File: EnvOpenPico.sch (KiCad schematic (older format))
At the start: 36 parts, among them J2 Conn_01x02, J3 Conn_02x18_Odd_Even, J4 Conn_02x18_Odd_Even, J5 Conn_01x03_Male, U1 NCP1117-3.3_SOT223, U2 W25Q16JVSSIQ, U3 RP2040, X1 XO32

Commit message: Changed Regulator for one with an enable pin
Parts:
- added R7: R100K, Resistor_SMD:R_0201_0603Metric, symbol Device:R
- R5, R6: footprint (none) -> Resistor_SMD:R_0201_0603Metric
- U1: value NCP1117-3.3_SOT223 -> SPX3819M5-L-3-3; footprint Package_TO_SOT_SMD:SOT-23 -> Package_TO_SOT_SMD:SOT-23-5; symbol Regulator_Linear:NCP1117-3.3_SOT223 -> Regulator_Linear:SPX3819M5-L-3-3
- U2: footprint Package_SO:SOIC-8_5.23x5.23mm_P1.27mm -> W25Q16JVSSIQ:SOIC127P790X216-8N
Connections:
- net labels added: 3V3_EN
- wire segments 182 -> 185
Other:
- moved on the sheet: C1
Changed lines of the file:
@@
 $EndComp
 $Comp
-L Regulator_Linear:NCP1117-3.3_SOT223 U1
+L Regulator_Linear:SPX3819M5-L-3-3 U1
 U 1 1 5F04C8B7
-P 3000 1750
-F 0 "U1" H 3000 1992 50  0000 C CNN
-F 1 "NCP1117-3.3_SOT223" H 3000 1901 50  0000 C CNN
-F 2 "Package_TO_SOT_SMD:SOT-23" H 3000 1950 50  0001 C CNN
-F 3 "http://www.onsemi.com/pub_link/Collateral/NCP1117-D.PDF" H 3100 1500 50  0001 C CNN
-	1    3000 1750
+P 3000 1850
+F 0 "U1" H 3000 2092 50  0000 C CNN
+F 1 "SPX3819M5-L-3-3" H 3000 2200 50  0000 C CNN
+F 2 "Package_TO_SOT_SMD:SOT-23-5" H 3000 2050 50  0001 C CNN
+F 3 "~" H 3100 1600 50  0001 C CNN
+	1    3000 1850
 	1    0    0    -1
 $EndComp
@@
 L power:GND #PWR05
 U 1 1 5F06A60B
-P 3000 2100
-F 0 "#PWR05" H 3000 1850 50  0001 C CNN
-F 1 "GND" H 2850 2050 50  0000 C CNN
-F 2 "" H 3000 2100 50  0001 C CNN
-F 3 "" H 3000 2100 50  0001 C CNN
-	1    3000 2100
-	1    0    0    -1
-$EndComp
-Wire Wire Line
-	3000 2050 3000 2100
+P 3000 2150
+F 0 "#PWR05" H 3000 1900 50  0001 C CNN
+F 1 "GND" H 2850 2100 50  0000 C CNN
+F 2 "" H 3000 2150 50  0001 C CNN
+F 3 "" H 3000 2150 50  0001 C CNN
+	1    3000 2150
+	1    0    0    -1
+$EndComp
 Wire Wire Line
 	3300 1750 3700 1750
@@
 L Device:C C1
 U 1 1 5F09255D
-P 2300 1950
-F 0 "C1" H 2415 1996 50  0000 L CNN
-F 1 "10u" H 2415 1905 50  0000 L CNN
-F 2 "Capacitor_SMD:C_0402_1005Metric" H 2338 1800 50  0001 C CNN
-F 3 "~" H 2300 1950 50  0001 C CNN
-	1    2300 1950
+P 2150 1950
+F 0 "C1" H 2265 1996 50  0000 L CNN
+F 1 "10u" H 2265 1905 50  0000 L CNN
+F 2 "Capacitor_SMD:C_0402_1005Metric" H 2188 1800 50  0001 C CNN
+F 3 "~" H 2150 1950 50  0001 C CNN
+	1    2150 1950
 	1    0    0    -1
 $EndComp
@@
 L power:GND #PWR04
 U 1 1 5F093D45
-P 2300 2150
-F 0 "#PWR04" H 2300 1900 50  0001 C CNN
-F 1 "GND" H 2150 2100 50  0000 C CNN
-F 2 "" H 2300 2150 50  0001 C CNN
-F 3 "" H 2300 2150 50  0001 C CNN
-	1    2300 2150
-	1    0    0    -1
-$EndComp
-Wire Wire Line
-	2300 2100 2300 2150
+P 2150 2150
+F 0 "#PWR04" H 2150 1900 50  0001 C CNN
+F 1 "GND" H 2000 2100 50  0000 C CNN
+F 2 "" H 2150 2150 50  0001 C CNN
+F 3 "" H 2150 2150 50  0001 C CNN
+	1    2150 2150
+	1    0    0    -1
+$EndComp
+Wire Wire Line
+	2150 2100 2150 2150
 $Comp
 L power:GND #PWR010
@@
 Wire Wire Line
 	3700 2100 3700 2150
-Wire Wire Line
-	2300 1800 2300 1750
 Wire Wire Line
 	3700 1800 3700 1750
@@
 F 0 "U2" H 3400 4400 50  0000 C CNN
 F 1 "W25Q16JVSSIQ" H 3400 4550 50  0000 C CNN
-F 2 "Package_SO:SOIC-8_5.23x5.23mm_P1.27mm" H 3400 5150 50  0001 L BNN
+F 2 "W25Q16JVSSIQ:SOIC127P790X216-8N" H 2650 4250 50  0000 L BNN
 F 3 "" H 3400 5150 50  0001 L BNN
 F 4 "Unavailable" H 3400 5150 50  0001 L BNN "AVAILABILITY"
@@
 Wire Wire Line
 	4300 5250 4700 5250
-Connection ~ 2500 4950
 Wire Wire Line
 	2050 4950 2500 4950
@@
 Wire Wire Line
 	1900 1700 1900 1750
-Wire Wire Line
-	2300 1750 2700 1750
-Wire Wire Line
-	1900 1750 2300 1750
-Connection ~ 2300 1750
 Wire Wire Line
 	14100 5200 14550 5200
@@
 F 0 "R6" V 1100 2100 50  0000 C CNN
 F 1 "5.1K" V 1200 2100 20  0000 C CNN
-F 2 "" H 1200 2100 50  0001 C CNN
+F 2 "Resistor_SMD:R_0201_0603Metric" H 1200 2100 50  0001 C CNN
 F 3 "~" H 1200 2100 50  0001 C CNN
 	1    1200 2100
@@
 F 0 "R5" V 1100 1500 50  0000 C CNN
 F 1 "5.1K" V 1200 1500 20  0000 C CNN
-F 2 "" H 1200 1500 50  0001 C CNN
+F 2 "Resistor_SMD:R_0201_0603Metric" H 1200 1500 50  0001 C CNN
 F 3 "~" H 1200 1500 50  0001 C CNN
 	1    1200 1500
@@
 	0    -1   -1   0
 $EndComp
+$Comp
+L logo:LOGO #G1
+U 1 1 608B0F05
+P 12150 10200
+F 0 "#G1" H 12150 10017 60  0001 C CNN
+F 1 "LOGO" H 12150 10383 60  0001 C CNN
+F 2 "EnvExtras:logo" H 12150 10200 50  0001 C CNN
+F 3 "" H 12150 10200 50  0001 C CNN
+	1    12150 10200
+	1    0    0    -1
+$EndComp
+Wire Wire Line
+	1900 1750 2150 1750
+Wire Wire Line
+	2150 1800 2150 1750
+Connection ~ 2150 1750
+Wire Wire Line
+	2150 1750 2500 1750
+$Comp
+L Device:R R7
+U 1 1 608CFAF0
+P 2500 1900
+F 0 "R7" H 2570 1946 50  0000 L CNN
+F 1 "R100K" H 2570 1855 50  0000 L CNN
+F 2 "Resistor_SMD:R_0201_0603Metric" V 2430 1900 50  0001 C CNN
+F 3 "~" H 2500 1900 50  0001 C CNN
+	1    2500 1900
+	1    0    0    -1
+$EndComp
+Connection ~ 2500 1750
+Wire Wire Line
+	2500 1750 2700 1750
+Wire Wire Line
+	2500 2050 2650 2050
+Wire Wire Line
+	2650 2050 2650 1850
+Wire Wire Line
+	2650 1850 2700 1850
+Text GLabel 14600 5000 0    50   Input ~ 0
+3V3_EN
+Text GLabel 2500 2050 3    50   Input ~ 0
+3V3_EN
 $EndSCHEMATC

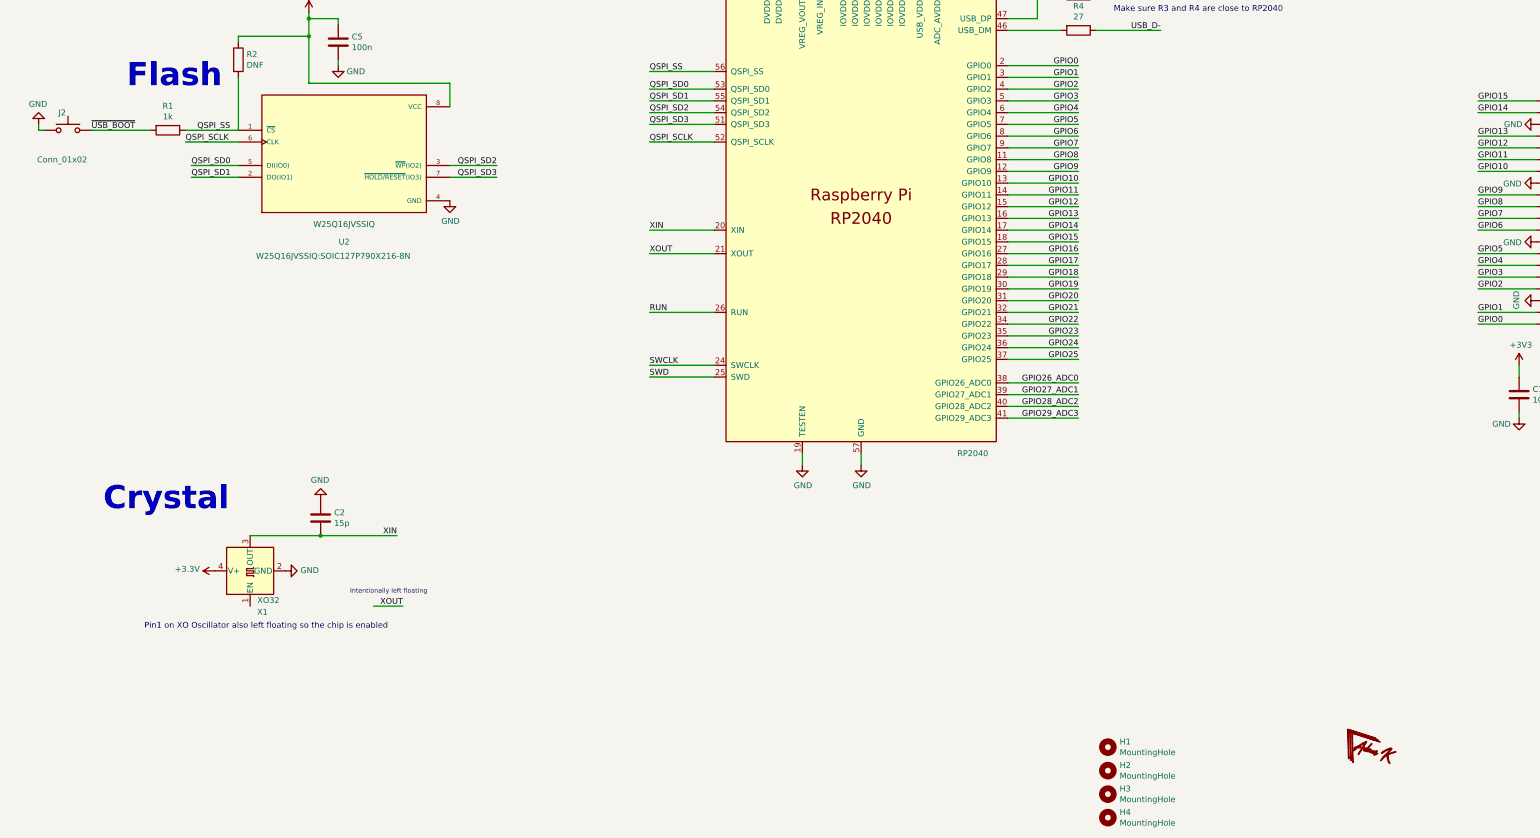
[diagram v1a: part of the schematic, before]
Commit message: Changed SOIC Flash for WSON Flash
also added a button instead of 1mm pitch headers along with general other track adjustments and stuff.
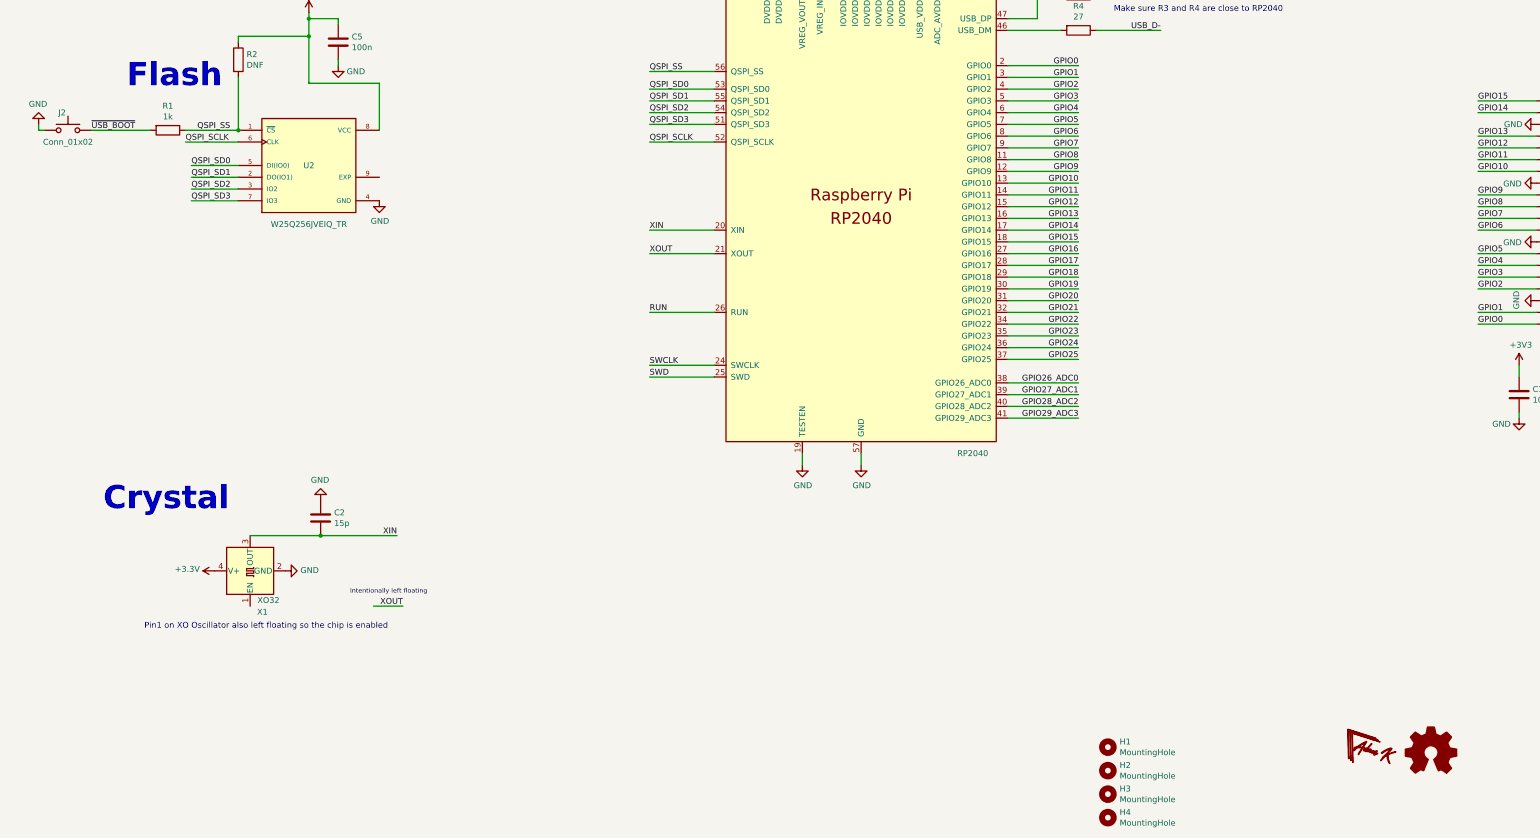
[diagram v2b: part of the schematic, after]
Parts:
- removed U2: W25Q16JVSSIQ, W25Q16JVSSIQ:SOIC127P790X216-8N, symbol W25Q16JVSSIQ:W25Q16JVSSIQ
- added U2: W25Q256JVEIQ_TR, SON127P800X600X80-9N, symbol W25Q256JVEIQ_TR:W25Q256JVEIQ_TR
- J2: footprint Connector_PinHeader_1.00mm:PinHeader_1x02_P1.00mm_Vertical -> Button_Switch_SMD:SW_SPST_B3U-1000P
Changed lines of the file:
@@
 P 1050 4950
 F 0 "J2" H 1100 5100 50  0000 C CNN
-F 1 "Conn_01x02" H 1100 4700 50  0000 C CNN
-F 2 "Connector_PinHeader_1.00mm:PinHeader_1x02_P1.00mm_Vertical" H 1050 4950 50  0001 C CNN
+F 1 "Conn_01x02" H 1050 4850 50  0000 C CNN
+F 2 "Button_Switch_SMD:SW_SPST_B3U-1000P" H 1050 4950 50  0001 C CNN
 F 3 "~" H 1050 4950 50  0001 C CNN
 	1    1050 4950
@@
 Text Label 14100 6900 0    50   ~ 0
 SWCLK
-$Comp
-L W25Q16JVSSIQ:W25Q16JVSSIQ U2
-U 1 1 608A7D5D
-P 3400 5150
-F 0 "U2" H 3400 4400 50  0000 C CNN
-F 1 "W25Q16JVSSIQ" H 3400 4550 50  0000 C CNN
-F 2 "W25Q16JVSSIQ:SOIC127P790X216-8N" H 2650 4250 50  0000 L BNN
-F 3 "" H 3400 5150 50  0001 L BNN
-F 4 "Unavailable" H 3400 5150 50  0001 L BNN "AVAILABILITY"
-F 5 "3v 16m-Bit Serial Flash Memory With Dual" H 3400 5150 50  0001 L BNN "DESCRIPTION"
-F 6 "W25Q16JVSSIQ" H 3400 5150 50  0001 L BNN "MP"
-F 7 "None" H 3400 5150 50  0001 L BNN "PRICE"
-F 8 "Winbond Electronics" H 3400 5150 50  0001 L BNN "MF"
-F 9 "SOIC-8 Winbond" H 3400 5150 50  0001 L BNN "PACKAGE"
-	1    3400 5150
-	1    0    0    -1
-$EndComp
 Text Label 2150 4950 0    50   ~ 0
 QSPI_SS
@@
 L power:GND #PWR0101
 U 1 1 608CFF74
-P 4300 5550
-F 0 "#PWR0101" H 4300 5300 50  0001 C CNN
-F 1 "GND" H 4305 5377 50  0000 C CNN
-F 2 "" H 4300 5550 50  0001 C CNN
-F 3 "" H 4300 5550 50  0001 C CNN
-	1    4300 5550
-	1    0    0    -1
-$EndComp
-Text Label 4700 5350 2    50   ~ 0
+P 3700 5550
+F 0 "#PWR0101" H 3700 5300 50  0001 C CNN
+F 1 "GND" H 3705 5377 50  0000 C CNN
+F 2 "" H 3700 5550 50  0001 C CNN
+F 3 "" H 3700 5550 50  0001 C CNN
+	1    3700 5550
+	1    0    0    -1
+$EndComp
+Text Label 2100 5550 0    50   ~ 0
 QSPI_SD3
-Text Label 4700 5250 2    50   ~ 0
+Text Label 2100 5450 0    50   ~ 0
 QSPI_SD2
 Text Label 2100 5250 0    50   ~ 0
@@
 	2100 5350 2500 5350
 Wire Wire Line
-	4300 5350 4700 5350
-Wire Wire Line
-	4300 5250 4700 5250
+	2500 5550 2100 5550
+Wire Wire Line
+	2500 5450 2100 5450
 Wire Wire Line
 	2050 4950 2500 4950
 Wire Wire Line
 	3100 4150 3100 4550
-Wire Wire Line
-	3100 4550 4300 4550
-Wire Wire Line
-	4300 4550 4300 4750
 Connection ~ 3100 4150
 Wire Wire Line
@@
 Text GLabel 2500 2050 3    50   Input ~ 0
 3V3_EN
+$Comp
+L W25Q256JVEIQ_TR:W25Q256JVEIQ_TR U2
+U 1 1 608EDADA
+P 3100 5250
+F 0 "U2" H 3100 5250 50  0000 C CNN
+F 1 "W25Q256JVEIQ_TR" H 3100 4750 50  0000 C CNN
+F 2 "SON127P800X600X80-9N" H 3100 5250 50  0001 L BNN
+F 3 "" H 3100 5250 50  0001 L BNN
+F 4 "Winbond Electronics Corp." H 3100 5250 50  0001 L BNN "MANUFACTURER"
+	1    3100 5250
+	1    0    0    -1
+$EndComp
+Connection ~ 2500 4950
+Wire Wire Line
+	3700 4950 3700 4550
+Wire Wire Line
+	3100 4550 3700 4550
+$Comp
+L Graphic:Logo_Open_Hardware_Small #LOGO1
+U 1 1 608CE996
+P 12650 10250
+F 0 "#LOGO1" H 12650 10525 50  0001 C CNN
+F 1 "Logo_Open_Hardware_Small" H 12650 10025 50  0001 C CNN
+F 2 "EnvExtras:logo" H 12650 10250 50  0001 C CNN
+F 3 "~" H 12650 10250 50  0001 C CNN
+	1    12650 10250
+	1    0    0    -1
+$EndComp
 $EndSCHEMATC

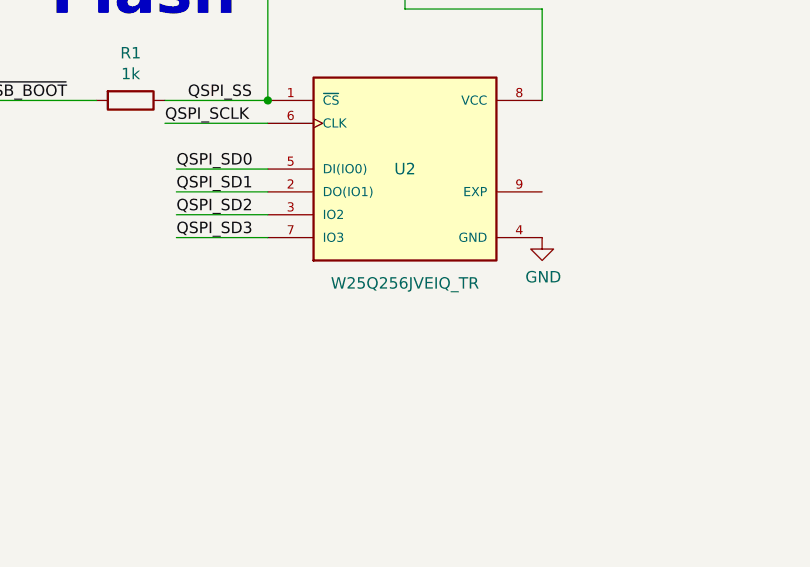
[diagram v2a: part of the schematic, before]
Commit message: Updated some components to be JLCPCB SMT Assembly compatible
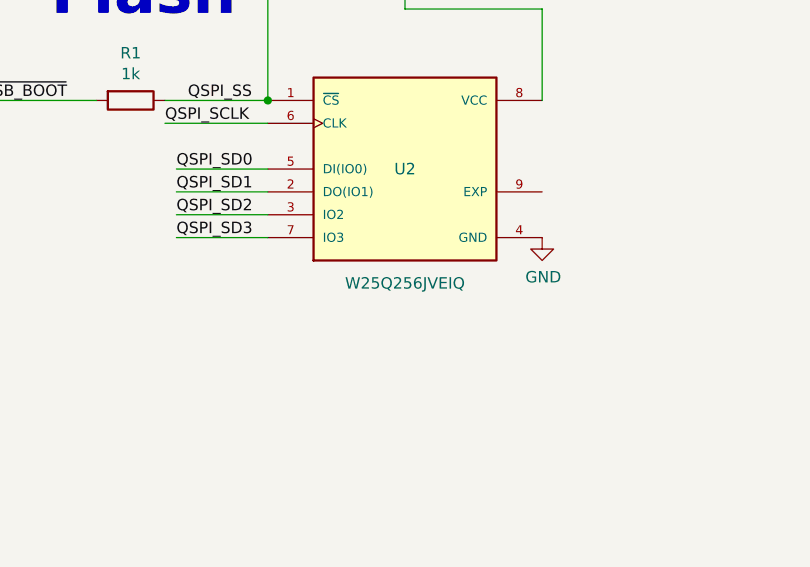
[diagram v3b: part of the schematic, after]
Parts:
- D2: footprint Diode_SMD:D_0402_1005Metric -> Diode_SMD:D_0603_1608Metric
- R5, R6, R7: footprint Resistor_SMD:R_0201_0603Metric -> Resistor_SMD:R_0402_1005Metric
- U2: value W25Q256JVEIQ_TR -> W25Q256JVEIQ; footprint SON127P800X600X80-9N -> (none)
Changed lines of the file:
@@
 F 0 "D2" H 15000 4900 50  0000 C CNN
 F 1 "D_Schottky" H 14850 5000 50  0000 C CNN
-F 2 "Diode_SMD:D_0402_1005Metric" H 14450 5100 50  0001 C CNN
+F 2 "Diode_SMD:D_0603_1608Metric" H 14450 5100 50  0001 C CNN
 F 3 "~" H 14450 5100 50  0001 C CNN
 	1    14450 5100
@@
 F 0 "R6" V 1100 2100 50  0000 C CNN
 F 1 "5.1K" V 1200 2100 20  0000 C CNN
-F 2 "Resistor_SMD:R_0201_0603Metric" H 1200 2100 50  0001 C CNN
+F 2 "Resistor_SMD:R_0402_1005Metric" H 1200 2100 50  0001 C CNN
 F 3 "~" H 1200 2100 50  0001 C CNN
 	1    1200 2100
@@
 F 0 "R5" V 1100 1500 50  0000 C CNN
 F 1 "5.1K" V 1200 1500 20  0000 C CNN
-F 2 "Resistor_SMD:R_0201_0603Metric" H 1200 1500 50  0001 C CNN
+F 2 "Resistor_SMD:R_0402_1005Metric" H 1200 1500 50  0001 C CNN
 F 3 "~" H 1200 1500 50  0001 C CNN
 	1    1200 1500
@@
 F 0 "R7" H 2570 1946 50  0000 L CNN
 F 1 "R100K" H 2570 1855 50  0000 L CNN
-F 2 "Resistor_SMD:R_0201_0603Metric" V 2430 1900 50  0001 C CNN
+F 2 "Resistor_SMD:R_0402_1005Metric" V 2430 1900 50  0001 C CNN
 F 3 "~" H 2500 1900 50  0001 C CNN
 	1    2500 1900
@@
 P 3100 5250
 F 0 "U2" H 3100 5250 50  0000 C CNN
-F 1 "W25Q256JVEIQ_TR" H 3100 4750 50  0000 C CNN
-F 2 "SON127P800X600X80-9N" H 3100 5250 50  0001 L BNN
+F 1 "W25Q256JVEIQ" H 3100 4750 50  0000 C CNN
+F 2 "" H 3100 5250 50  0001 L BNN
 F 3 "" H 3100 5250 50  0001 L BNN
 F 4 "Winbond Electronics Corp." H 3100 5250 50  0001 L BNN "MANUFACTURER"
